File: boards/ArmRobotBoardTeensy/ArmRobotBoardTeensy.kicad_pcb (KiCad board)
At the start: 2 copper layers, 87.5 x 55 mm, 49 parts, among them J1 B5B-XH-A, J10 B4B-XH-A, J11 B3B-XH-A, J2 B4B-XH-A, J3 B3B-XH-A, J4 B3B-XH-A, J5 B4B-XH-A, J6 B2B-XH-A, J7 B2B-XH-A, J8 B4B-XH-A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

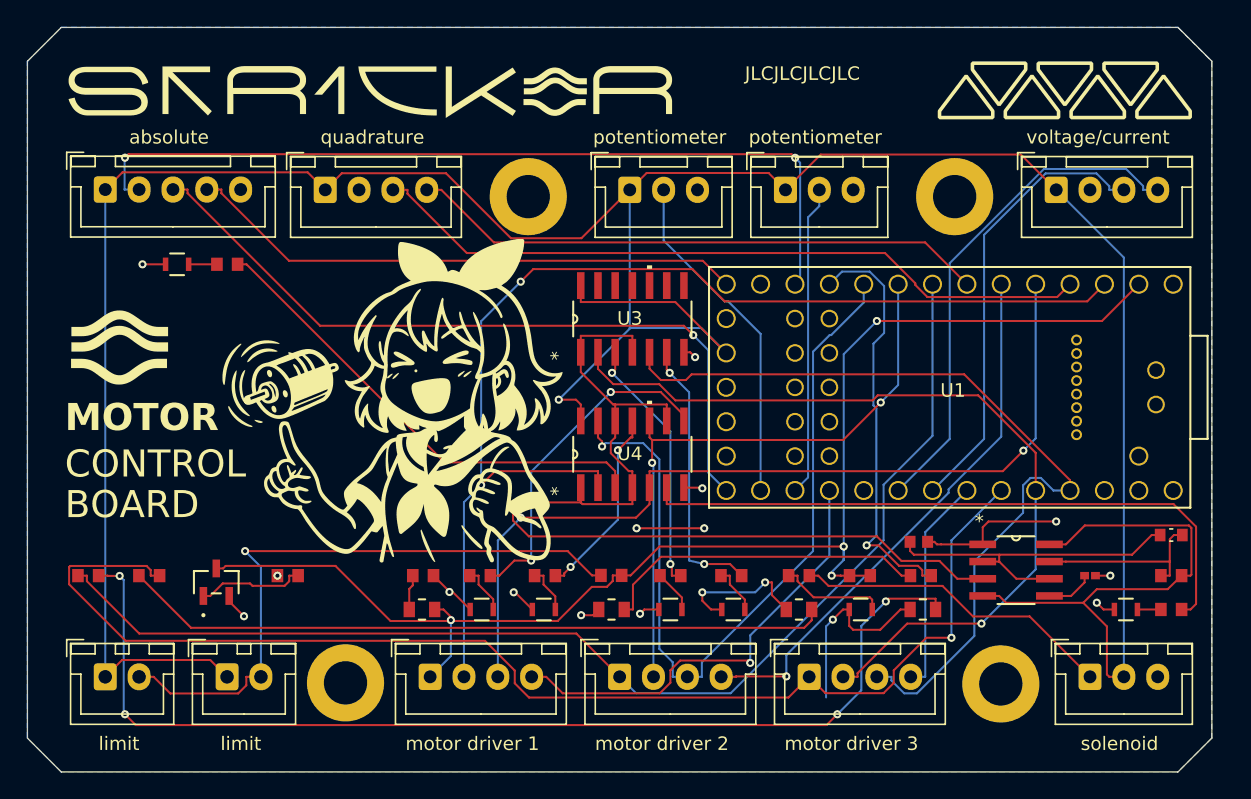
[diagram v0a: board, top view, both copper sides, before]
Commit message: Address ERC and DRC violations
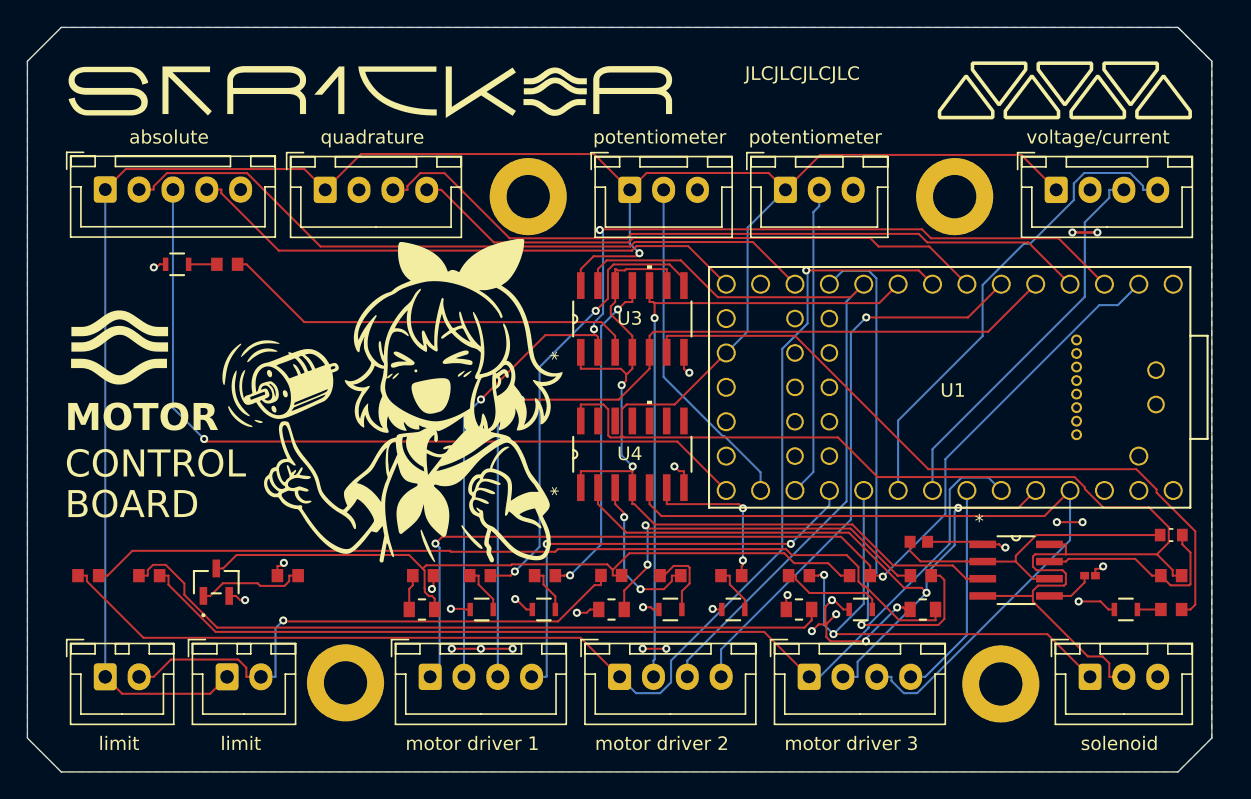
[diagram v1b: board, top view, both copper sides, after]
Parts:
- C1: value CC0603JRX7R7BB105 -> 1uF
- C2: value C0402C103J4RACTU -> 0.01uF
- D1, D2, D3, D4, D6, D7, D9: value 150080BS75000 -> BLUE LED
- D10, D11, D5, D8: value XL-2012SURC -> PINK LED
- R1, R10, R11, R12, R13, R2, R3, R4, R5, R6, R7, R9: value RCG06031K00FKEA -> 1K
- R14: value CRCW0603100KFKEA -> 100K
- R15, R8: value CRCW060310K0FKEA -> 10K
- R16: value RC0603FR-07360KL -> 360K
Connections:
- D5 pad 2: PWM1EN -> Net-(Q1-COLLECTOR)
- Q1 pad 3: PWM1EN -> Net-(Q1-COLLECTOR)
- R8 pad 2: PWM1EN -> Net-(Q1-COLLECTOR)
- R9 pad 1: PWM1EN -> Net-(Q1-COLLECTOR)
- U1 pad 24: SOL -> SIG
- U3 pad 10: unconnected-(GATE2-3B-Pad10) -> RPWM2
- U3 pad 11: unconnected-(GATE2-4Y-Pad11) -> LPWM2A
- U3 pad 12: unconnected-(GATE2-4A-Pad12) -> BLINK
- U3 pad 13: unconnected-(GATE2-4B-Pad13) -> LPWM2
- U3 pad 2: RPWM3 -> RPWM1
- U3 pad 3: RPWM3A -> RPWM1A
- U3 pad 5: LPWM3 -> LPWM1
- U3 pad 6: LPWM3A -> LPWM1A
- U3 pad 8: unconnected-(GATE2-3Y-Pad8) -> RPWM2A
- U3 pad 9: unconnected-(GATE2-3A-Pad9) -> BLINK
- U4 pad 10: RPWM2 -> unconnected-(U4-3B-Pad10)
- U4 pad 11: LPWM2A -> unconnected-(U4-4Y-Pad11)
- U4 pad 12: BLINK -> unconnected-(U4-4A-Pad12)
- U4 pad 13: LPWM2 -> unconnected-(U4-4B-Pad13)
- U4 pad 2: RPWM1 -> RPWM3
- U4 pad 3: RPWM1A -> RPWM3A
- U4 pad 5: LPWM1 -> LPWM3
- U4 pad 6: LPWM1A -> LPWM3A
- U4 pad 8: RPWM2A -> unconnected-(U4-3Y-Pad8)
- U4 pad 9: BLINK -> unconnected-(U4-3A-Pad9)
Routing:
- net Net-(Q1-COLLECTOR): track 0.00 -> 53.7 mm
- net PWM1EN: track 101.7 -> 75.4 mm, vias 4 -> 2
- net PWM3EN: track 93.5 -> 74.6 mm, vias 1 -> 0
- net SIG: track 23.8 -> 37.6 mm, vias 0 -> 2
- net Net-(D10-Pad2): track 79.6 -> 66.3 mm, vias 4 -> 0
- net RPWM3: track 62.7 -> 51.1 mm, vias 1 -> 2
- net LPWM2A: track 14.2 -> 24.7 mm
- net CS: track 62.8 -> 52.8 mm, vias 2 -> 0
- net BLINK: track 71.8 -> 61.9 mm, vias 0 -> 2
- net SPIS: track 30.7 -> 40.5 mm
- net GND: track 57.6 -> 48.4 mm, vias 17 -> 29
- net RPWM2A: track 24.9 -> 33.8 mm
- net LPWM3A: track 20.3 -> 12.0 mm
- net RPWM3A: track 19.1 -> 11.9 mm
- net LPWM3: track 63.1 -> 56.7 mm
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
